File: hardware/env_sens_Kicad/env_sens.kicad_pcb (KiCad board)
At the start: 2 copper layers, 60 x 60 mm, 40 parts, among them J1 CO2_Conn, J2 BATTERY, J3 USB_C_Receptacle_USB2.0_14P, J4 CAN_BUS, SW1 RESET, SW2 BOOT, U1 HDC1080, U2 TCAN1043xDxQ1, U3 ESP32-S3-WROOM-1, U6 TPD1E05U06DYA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

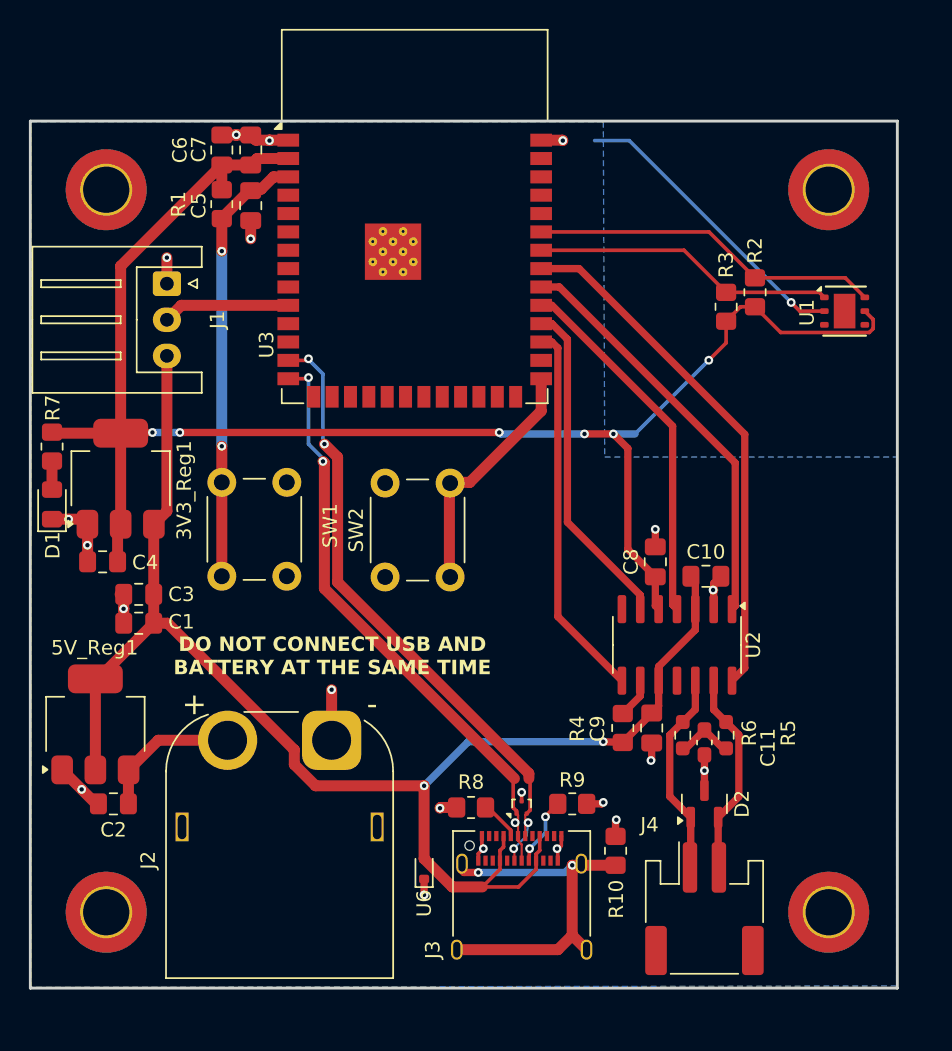
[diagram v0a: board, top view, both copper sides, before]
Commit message: Added central power source configuration from mother board
Central power source configuration from mother board + safety regulation
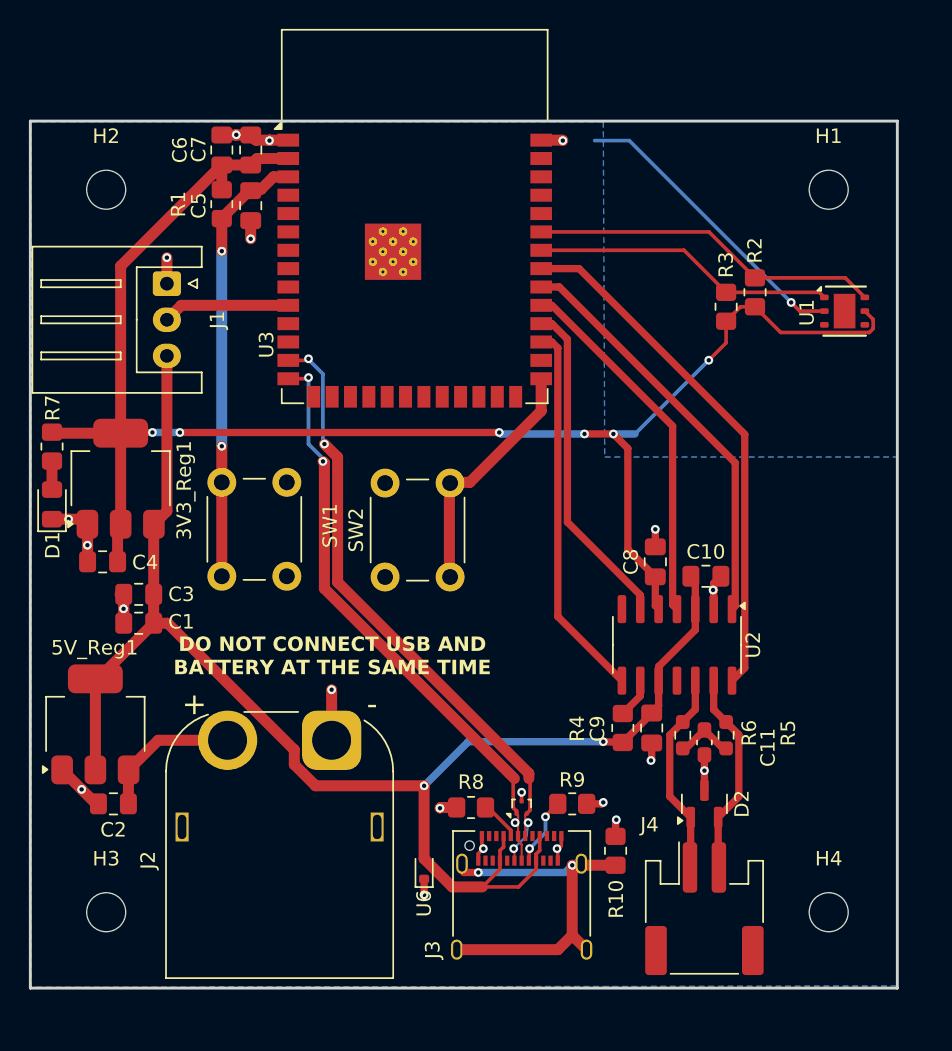
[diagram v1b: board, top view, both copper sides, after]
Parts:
- H1, H2, H3, H4: footprint MountingHole:MountingHole_3.2mm_M3_DIN965_Pad_TopBottom -> MountingHole:MountingHole_2.7mm_M2.5

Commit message: Updated layout with schematic changes
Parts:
- removed C11: 4.7n, Capacitor_SMD:C_0603_1608Metric_Pad1.08x0.95mm_HandSolder
- removed R5, R6: 60, Resistor_SMD:R_0603_1608Metric_Pad0.98x0.95mm_HandSolder
- added D3: D, Diode_SMD:D_SOD-123F, F.Cu at (45.2, 52.3)
- added D4: D, Diode_SMD:D_SOD-123F, F.Cu at (78.7, 66.2)
- added D5: D, Diode_SMD:D_SOD-123F, F.Cu at (58.6, 61.9)
- added J5: Conn_01x02_Pin, Connector_JST:JST_EH_S2B-EH_1x02_P2.50mm_Horizontal, F.Cu at (80.0, 70.2)
- added J6: CAN_BUS_in, Connector_JST:JST_EH_S2B-EH_1x02_P2.50mm_Horizontal, F.Cu at (87.3, 50.1)
- J2: footprint Connector_AMASS:AMASS_XT60PW-M_1x02_P7.20mm_Horizontal -> Connector_AMASS:AMASS_XT30PW-M_1x02_P2.50mm_Horizontal
- J4: value CAN_BUS -> CAN_BUS_out; footprint Connector_JST:JST_PH_S2B-PH-SM4-TB_1x02-1MP_P2.00mm_Horizontal -> Connector_JST:JST_EH_S2B-EH_1x02_P2.50mm_Horizontal
- moved J4 13.8 mm to (87.3, 59.1), turned to -90 degrees
- moved D2 12.9 mm to (81.5, 51.3), turned to 180 degrees
- moved C10 11.3 mm to (70.3, 51.2), turned to 90 degrees
- moved C8 11.1 mm to (69.3, 54.7), turned to 180 degrees
- moved J2 8.51 mm to (47.8, 63.8)
- moved R4 5.64 mm to (80.8, 57.0), turned to 180 degrees
- moved C9 5.18 mm to (80.8, 55.0), turned to 0 degrees
- moved U2 4.23 mm to (75.0, 53.2), turned to 0 degrees
- moved J3 3.11 mm to (65.4, 71.7)
- moved R10 3.11 mm to (71.9, 67.7)
- moved R8 3.11 mm to (61.9, 64.7)
- moved R9 3.11 mm to (68.9, 64.4)
- moved U6 3.11 mm to (58.6, 68.9)
- moved U7 3.11 mm to (65.4, 64.7)
- moved C1 1.40 mm to (42.0, 53.1)
- renumbered 5V_Reg1 to 5V_Reg
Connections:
- 5V_Reg pad 2: +5V -> +5V_reg
- C1 pad 1: +5V -> +5V_reg
- J3 pad A4: +5V -> +5V_usb
- J3 pad A9: +5V -> +5V_usb
- J3 pad B4: +5V -> +5V_usb
- J3 pad B9: +5V -> +5V_usb
- J4 pad 1: /CANL -> /CANH
- J4 pad 2: /CANH -> /CANL
- U6 pad 2: +5V -> +5V_usb
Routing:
- net +5V: track 104.2 -> 81.5 mm
- net +5V_usb: track 0.00 -> 20.6 mm
- net +5V_reg: track 0.00 -> 13.8 mm
- net /CAN_FAULTn: track 26.2 -> 39.0 mm
- net /CAN_EN: track 23.0 -> 33.8 mm
- net /CAN_STBn: track 36.3 -> 26.1 mm
- net /CANH: track 14.3 -> 21.0 mm
- net /CANL: track 14.5 -> 21.1 mm, vias 0 -> 2
- net +3V3: track 114.8 -> 121.1 mm, vias 6 -> 7
- net /Vbat: track 10.1 -> 16.1 mm
- net /CAN_RX: track 25.4 -> 30.0 mm
- net Net-(C11-Pad1): track 4.06 -> 0.00 mm
- net +5V_mb: track 0.00 -> 3.99 mm
- net /CAN_TX: track 28.7 -> 25.6 mm
- net GND: track 61.8 -> 58.7 mm, vias 22 -> 21
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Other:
- board text removed: "DO NOT CONNECT USB AND BATTERY AT THE SAME TIME"

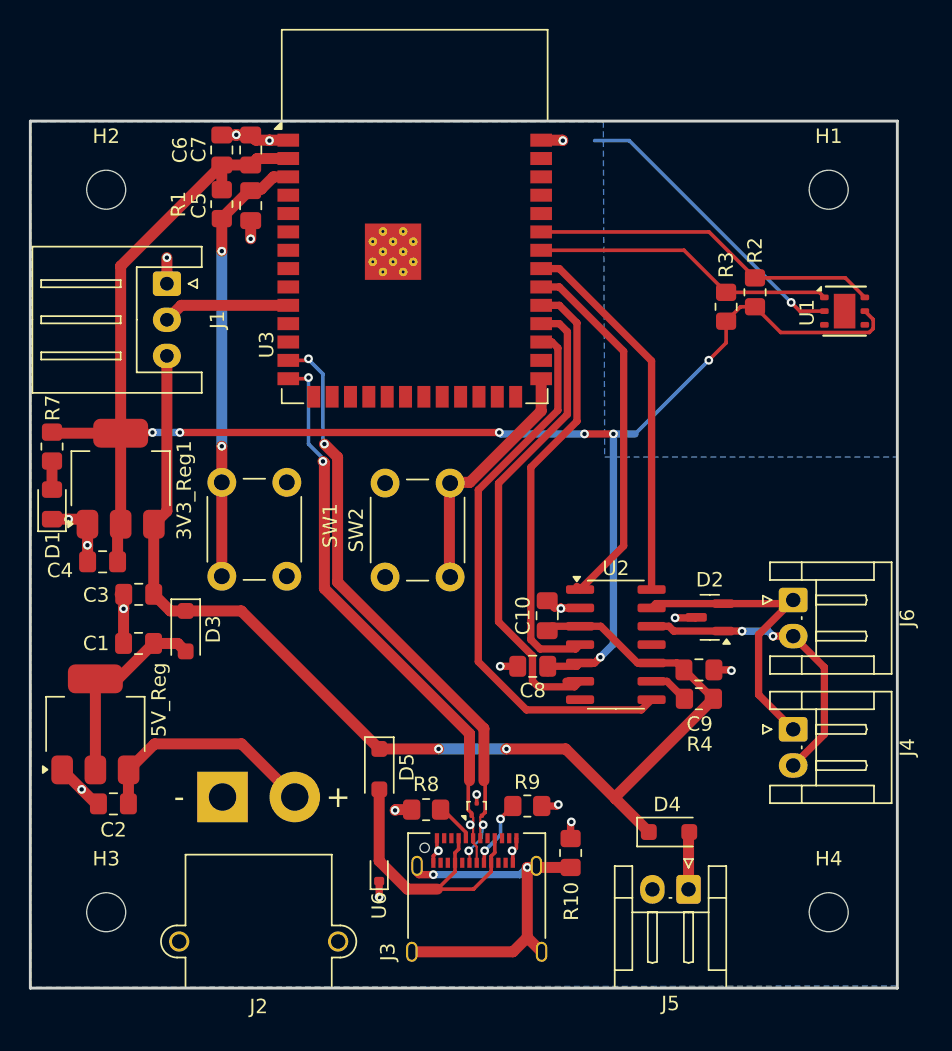
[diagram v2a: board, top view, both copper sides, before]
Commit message: Replaced with schottkey dioides & did production files
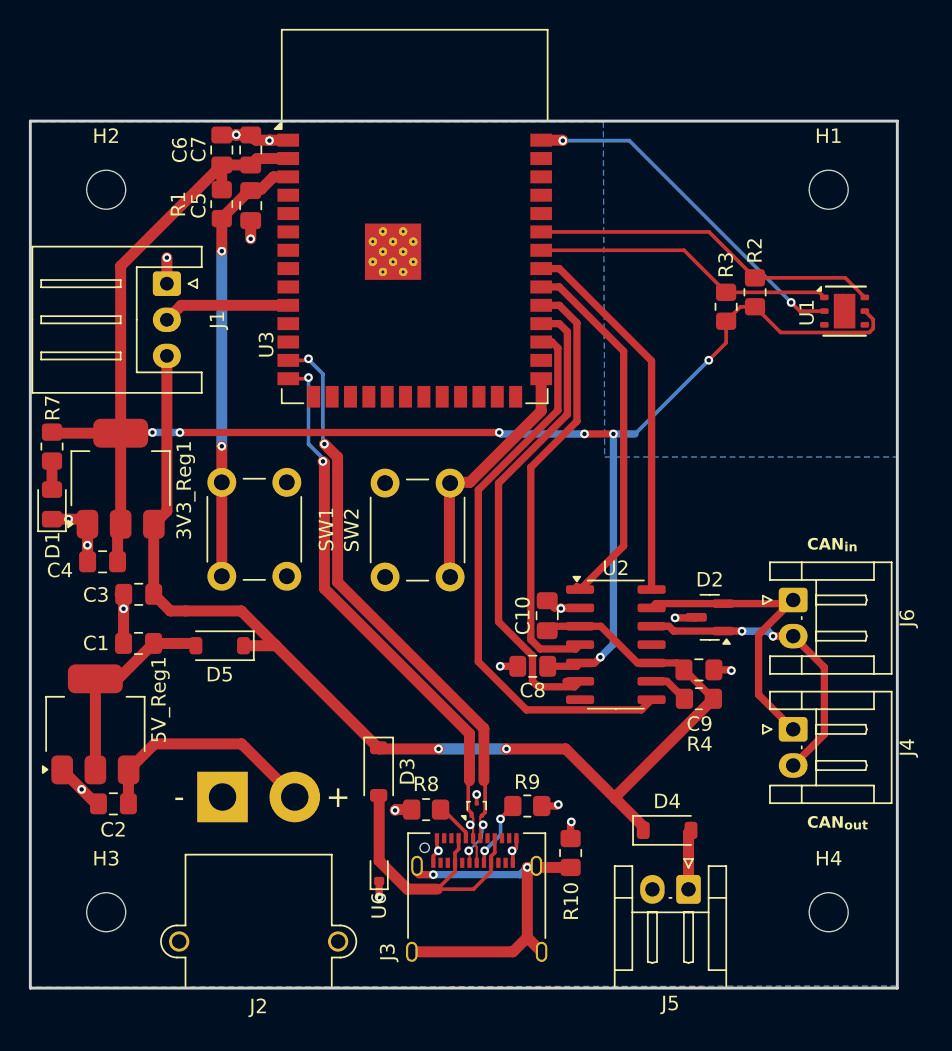
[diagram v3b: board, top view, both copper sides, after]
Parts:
- D3, D4, D5: value D -> D_Schottky; footprint Diode_SMD:D_SOD-123F -> Diode_SMD:D_SOD-123
- moved D3 16.5 mm to (58.6, 62.0)
- moved D5 14.0 mm to (47.6, 53.3), turned to 180 degrees
- moved D4 0.17 mm to (78.6, 66.1)
- renumbered 5V_Reg to 5V_Reg1
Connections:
- D3 pad 2: +5V_reg -> +5V_usb
- D5 pad 2: +5V_usb -> +5V_reg
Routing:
- net GND: track 58.7 -> 60.9 mm
- net +5V: track 81.5 -> 83.4 mm
- net +5V_reg: track 13.8 -> 14.3 mm
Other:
- board text added: "CAN_{in}"
- board text added: "CAN_{out}"
